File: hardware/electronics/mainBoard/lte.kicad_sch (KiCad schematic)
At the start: 39 parts, among them J10 M.2 Standoff, J8 Bus_M.2_Socket_E, J9 M.2 Standoff, SW5 JS102011JCQN, SW6 JS102011JCQN, U10 TPS22996H-Q1, U11 TXS0108EQWRKSRQ1, U12 TXS0104VxRUTR

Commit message: redefined symbol refs
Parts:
- renumbered D7 to D5, JP4 to JP2, R41 to R39, R42 to R40, R43 to R41, R44 to R42
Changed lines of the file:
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@@
 		(dnp no)
 		(fields_autoplaced yes)
-		(property "Reference" "#PWR0147"
+		(property "Reference" "#PWR0145"
 			(at 55.88 184.15 0)
 			(effects
@@
 			(project "mainBoard"
 				(path "/be16e32f-2ccf-4272-9ec7-94d5fe7a55e0/7ff6c767-11c2-4c6d-a16f-82c26617ef6d"
-					(reference "#PWR0147")
+					(reference "#PWR0145")
 					(unit 1)
 				)
@@
 		(dnp no)
 		(fields_autoplaced yes)
-		(property "Reference" "#PWR0150"
+		(property "Reference" "#PWR0148"
 			(at 127 191.77 0)
 			(effects
@@
 			(project "mainBoard"
 				(path "/be16e32f-2ccf-4272-9ec7-94d5fe7a55e0/7ff6c767-11c2-4c6d-a16f-82c26617ef6d"
-					(reference "#PWR0150")
+					(reference "#PWR0148")
 					(unit 1)
 				)
@@
 		(dnp no)
 		(fields_autoplaced yes)
-		(property "Reference" "#PWR0151"
+		(property "Reference" "#PWR0149"
 			(at 152.4 191.77 0)
 			(effects
@@
 			(project "mainBoard"
 				(path "/be16e32f-2ccf-4272-9ec7-94d5fe7a55e0/7ff6c767-11c2-4c6d-a16f-82c26617ef6d"
-					(reference "#PWR0151")
+					(reference "#PWR0149")
 					(unit 1)
 				)
@@
 		(dnp no)
 		(fields_autoplaced yes)
-		(property "Reference" "#PWR0130"
+		(property "Reference" "#PWR0129"
 			(at 200.66 27.94 0)
 			(effects
@@
 			(project "mainBoard"
 				(path "/be16e32f-2ccf-4272-9ec7-94d5fe7a55e0/7ff6c767-11c2-4c6d-a16f-82c26617ef6d"
-					(reference "#PWR0130")
+					(reference "#PWR0129")
 					(unit 1)
 				)
@@
 		(dnp no)
 		(fields_autoplaced yes)
-		(property "Reference" "#PWR0131"
+		(property "Reference" "#PWR0130"
 			(at 180.34 30.48 0)
 			(effects
@@
 			(project ""
 				(path "/be16e32f-2ccf-4272-9ec7-94d5fe7a55e0/7ff6c767-11c2-4c6d-a16f-82c26617ef6d"
-					(reference "#PWR0131")
+					(reference "#PWR0130")
 					(unit 1)
 				)
@@
 		(dnp no)
 		(fields_autoplaced yes)
-		(property "Reference" "#PWR0145"
+		(property "Reference" "#PWR0143"
 			(at 139.7 157.48 0)
 			(effects
@@
 			(project "mainBoard"
 				(path "/be16e32f-2ccf-4272-9ec7-94d5fe7a55e0/7ff6c767-11c2-4c6d-a16f-82c26617ef6d"
-					(reference "#PWR0145")
+					(reference "#PWR0143")
 					(unit 1)
 				)
@@
 		(dnp no)
 		(fields_autoplaced yes)
-		(property "Reference" "R42"
+		(property "Reference" "R40"
 			(at 199.39 34.29 0)
 			(do_not_autoplace yes)
@@
 			(project "mainBoard"
 				(path "/be16e32f-2ccf-4272-9ec7-94d5fe7a55e0/7ff6c767-11c2-4c6d-a16f-82c26617ef6d"
-					(reference "R42")
+					(reference "R40")
 					(unit 1)
 				)
@@
 		(dnp no)
 		(fields_autoplaced yes)
-		(property "Reference" "#PWR0148"
+		(property "Reference" "#PWR0146"
 			(at 30.48 191.77 0)
 			(effects
@@
 			(project "mainBoard"
 				(path "/be16e32f-2ccf-4272-9ec7-94d5fe7a55e0/7ff6c767-11c2-4c6d-a16f-82c26617ef6d"
-					(reference "#PWR0148")
+					(reference "#PWR0146")
 					(unit 1)
 				)
@@
 		(dnp no)
 		(fields_autoplaced yes)
-		(property "Reference" "#PWR0146"
+		(property "Reference" "#PWR0144"
 			(at 30.48 184.15 0)
 			(effects
@@
 			(project "mainBoard"
 				(path "/be16e32f-2ccf-4272-9ec7-94d5fe7a55e0/7ff6c767-11c2-4c6d-a16f-82c26617ef6d"
-					(reference "#PWR0146")
+					(reference "#PWR0144")
 					(unit 1)
 				)
@@
 		(dnp no)
 		(fields_autoplaced yes)
-		(property "Reference" "#PWR0129"
+		(property "Reference" "#PWR0128"
 			(at 203.2 19.05 0)
 			(effects
@@
 			(project ""
 				(path "/be16e32f-2ccf-4272-9ec7-94d5fe7a55e0/7ff6c767-11c2-4c6d-a16f-82c26617ef6d"
-					(reference "#PWR0129")
+					(reference "#PWR0128")
 					(unit 1)
 				)
@@
 		(dnp no)
 		(fields_autoplaced yes)
-		(property "Reference" "#PWR0149"
+		(property "Reference" "#PWR0147"
 			(at 55.88 191.77 0)
 			(effects
@@
 			(project "mainBoard"
 				(path "/be16e32f-2ccf-4272-9ec7-94d5fe7a55e0/7ff6c767-11c2-4c6d-a16f-82c26617ef6d"
-					(reference "#PWR0149")
+					(reference "#PWR0147")
 					(unit 1)
 				)
@@
 		(dnp no)
 		(fields_autoplaced yes)
-		(property "Reference" "D7"
+		(property "Reference" "D5"
 			(at 255.27 38.735 0)
 			(do_not_autoplace yes)
@@
 			(project "mainBoard"
 				(path "/be16e32f-2ccf-4272-9ec7-94d5fe7a55e0/7ff6c767-11c2-4c6d-a16f-82c26617ef6d"
-					(reference "D7")
+					(reference "D5")
 					(unit 1)
 				)
@@
 		(dnp no)
 		(fields_autoplaced yes)
-		(property "Reference" "R43"
+		(property "Reference" "R41"
 			(at 199.39 44.45 0)
 			(do_not_autoplace yes)
@@
 			(project "mainBoard"
 				(path "/be16e32f-2ccf-4272-9ec7-94d5fe7a55e0/7ff6c767-11c2-4c6d-a16f-82c26617ef6d"
-					(reference "R43")
+					(reference "R41")
 					(unit 1)
 				)
@@
 		(on_board yes)
 		(dnp no)
-		(property "Reference" "JP4"
+		(property "Reference" "JP2"
 			(at 255.27 55.88 90)
 			(do_not_autoplace yes)
@@
 			(project "mainBoard"
 				(path "/be16e32f-2ccf-4272-9ec7-94d5fe7a55e0/7ff6c767-11c2-4c6d-a16f-82c26617ef6d"
-					(reference "JP4")
+					(reference "JP2")
 					(unit 1)
 				)
@@
 		(dnp no)
 		(fields_autoplaced yes)
-		(property "Reference" "R41"
+		(property "Reference" "R39"
 			(at 88.9 25.4 0)
 			(do_not_autoplace yes)
@@
 			(project "mainBoard"
 				(path "/be16e32f-2ccf-4272-9ec7-94d5fe7a55e0/7ff6c767-11c2-4c6d-a16f-82c26617ef6d"
-					(reference "R41")
+					(reference "R39")
 					(unit 1)
 				)
@@
 		(dnp no)
 		(fields_autoplaced yes)
-		(property "Reference" "#PWR0120"
+		(property "Reference" "#PWR0131"
 			(at 228.6 40.64 0)
 			(effects
@@
 			(project "mainBoard"
 				(path "/be16e32f-2ccf-4272-9ec7-94d5fe7a55e0/7ff6c767-11c2-4c6d-a16f-82c26617ef6d"
-					(reference "#PWR0120")
+					(reference "#PWR0131")
 					(unit 1)
 				)
@@
 		(dnp no)
 		(fields_autoplaced yes)
-		(property "Reference" "R44"
+		(property "Reference" "R42"
 			(at 255.27 45.72 0)
 			(do_not_autoplace yes)
@@
 			(project "mainBoard"
 				(path "/be16e32f-2ccf-4272-9ec7-94d5fe7a55e0/7ff6c767-11c2-4c6d-a16f-82c26617ef6d"
-					(reference "R44")
+					(reference "R42")
 					(unit 1)
 				)

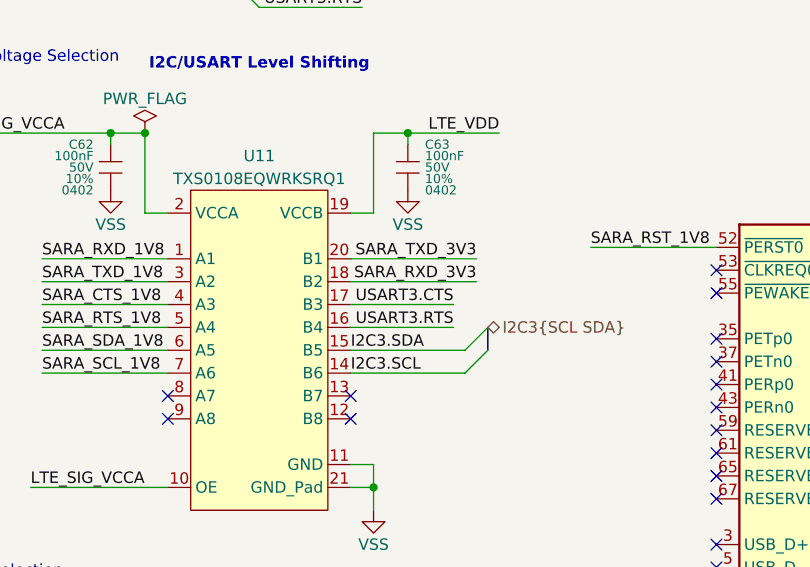
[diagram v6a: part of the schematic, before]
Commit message: fixed rx/tx
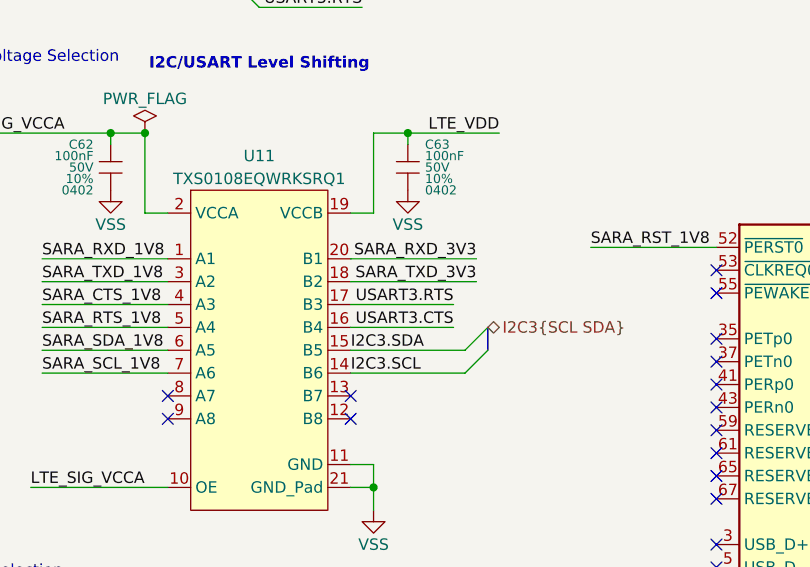
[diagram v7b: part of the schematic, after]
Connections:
- net SARA_RXD_3V3: now also U11.20 (B1); no longer U11.18 (B2)
- net SARA_TXD_3V3: now also U11.18 (B2); no longer U11.20 (B1)
- net USART3.CTS: now also U11.16 (B4); no longer U11.17 (B3)
- net USART3.RTS: now also U11.17 (B3); no longer U11.16 (B4)
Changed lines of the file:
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@@
-		)
-	)
-	(label "SARA_RXD_3V3"
-		(at 87.63 68.58 180)
-		(effects
-			(font
-				(size 1.27 1.27)
-			)
-			(justify right bottom)
 		)
 	)
@@
 		)
 	)
-	(label "USART3.RTS"
-		(at 85.09 73.66 180)
-		(effects
-			(font
-				(size 1.27 1.27)
-			)
-			(justify right bottom)
-		)
-	)
 	(label "LTE.SLEEP"
 		(at 86.36 125.73 180)
@@
 		)
 	)
-	(label "SARA_TXD_3V3"
-		(at 87.63 66.04 180)
-		(effects
-			(font
-				(size 1.27 1.27)
-			)
-			(justify right bottom)
-		)
-	)
 	(label "SARA_RST_1V8"
 		(at 100.33 64.77 0)
@@
 		)
 	)
+	(label "USART3.RTS"
+		(at 85.09 71.12 180)
+		(effects
+			(font
+				(size 1.27 1.27)
+			)
+			(justify right bottom)
+		)
+	)
 	(label "SARA_SCL_1V8"
 		(at 39.37 179.07 180)
@@
 		)
 	)
+	(label "SARA_TXD_3V3"
+		(at 87.63 68.58 180)
+		(effects
+			(font
+				(size 1.27 1.27)
+			)
+			(justify right bottom)
+		)
+	)
 	(label "LTE_1V8"
 		(at 236.22 35.56 180)
@@
 		)
 	)
+	(label "USART3.CTS"
+		(at 85.09 73.66 180)
+		(effects
+			(font
+				(size 1.27 1.27)
+			)
+			(justify right bottom)
+		)
+	)
 	(label "SARA_SLEEP_1V8"
 		(at 34.29 125.73 0)
@@
 		)
 	)
-	(label "USART3.CTS"
-		(at 85.09 71.12 180)
-		(effects
-			(font
-				(size 1.27 1.27)
-			)
-			(justify right bottom)
-		)
-	)
 	(label "LTE.NET_STS"
 		(at 40.64 26.67 180)
@@
 		(effects
 			(font
+				(size 1.27 1.27)
+			)
+			(justify right bottom)
+		)
+	)
+	(label "SARA_RXD_3V3"
+		(at 87.63 66.04 180)
+		(effects
+			(font

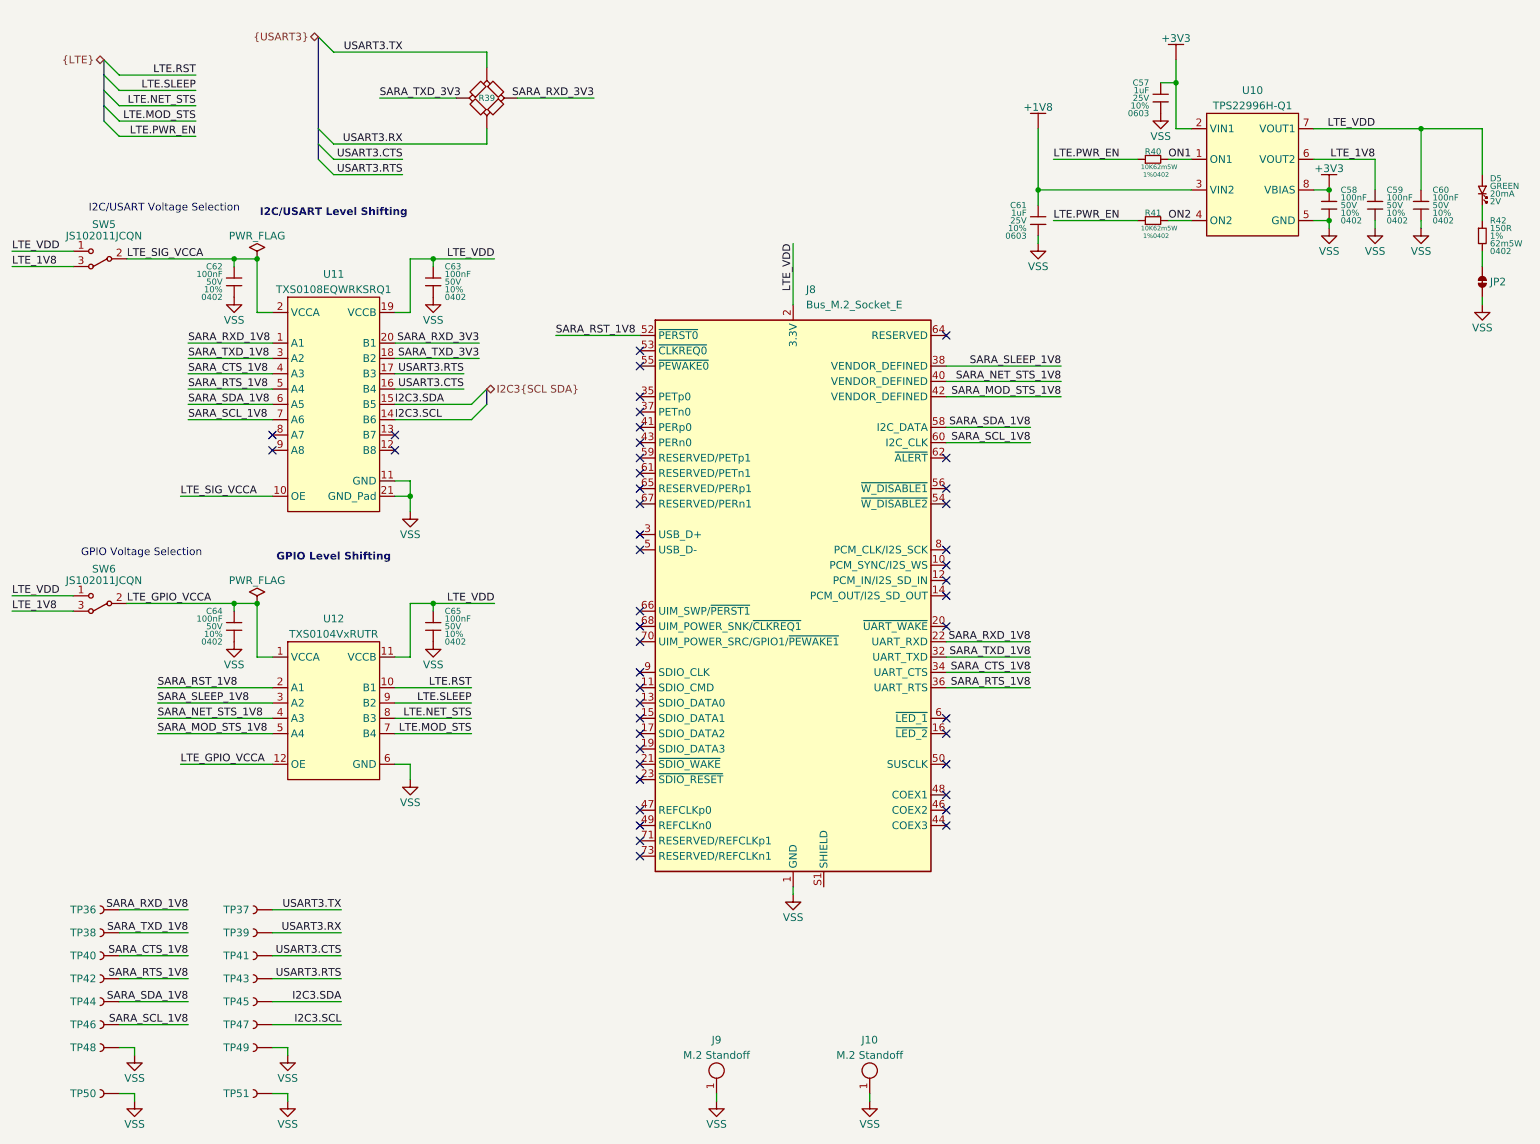
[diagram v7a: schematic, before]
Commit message: fixed net names and added notes
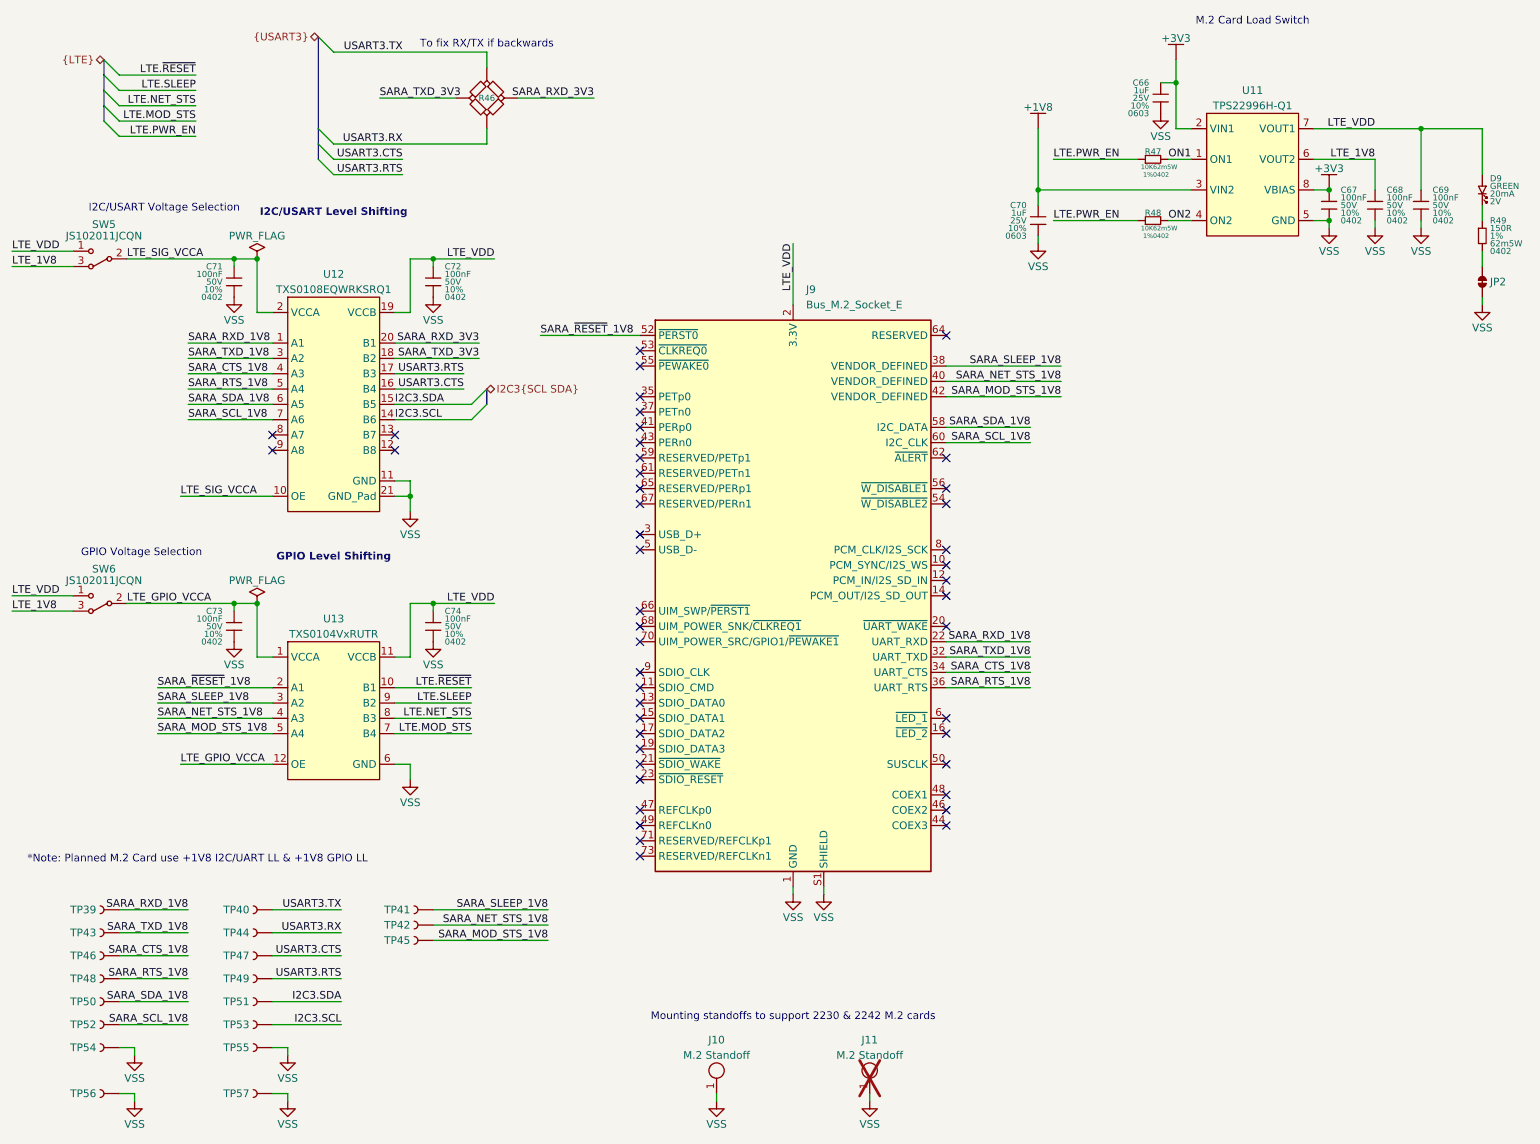
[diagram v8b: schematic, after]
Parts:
- removed R39: ~, lib_passives:CRCW0402_QUAD_UART, symbol lib_sch:R_double
- added R46: 0R, lib_passives:CRCW0402_QUAD_UART, symbol lib_sch:R_double
- added TP41, TP42, TP45: RCWCTE, lib_misc:TP_RCW, symbol lib_sch:Testpoint
- J11: renamed from J10; now not fitted
- renumbered C57 to C66, C58 to C67, C59 to C68, C60 to C69, C61 to C70, C62 to C71, C63 to C72, C64 to C73, C65 to C74, D5 to D9, J9 to J10, J8 to J9, R40 to R47, R41 to R48, R42 to R49, TP36 to TP39, TP37 to TP40, TP38 to TP43, TP39 to TP44, TP40 to TP46, TP41 to TP47, TP42 to TP48, TP43 to TP49, TP44 to TP50, TP45 to TP51, TP46 to TP52, TP47 to TP53, TP48 to TP54, TP49 to TP55, TP50 to TP56, TP51 to TP57, U10 to U11, U11 to U12, U12 to U13
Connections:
- net SARA_MOD_STS_1V8: now also TP45.1
- net SARA_NET_STS_1V8: now also TP42.1
- net SARA_RXD_3V3: now also R46.2
- net SARA_SLEEP_1V8: now also TP41.1
- net SARA_TXD_3V3: now also R46.4
- net USART3.RX: now also R46.3
- net USART3.TX: now also R46.1
- net VSS: now also J9.S1 (SHIELD), J9.S2 (SHIELD)
- net LTE.RST renamed LTE.~{RESET}
- net SARA_RST_1V8 renamed SARA_~{RESET}_1V8
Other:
- note added: "*Note: Planned M.2 Card use +1V8 I2C/UART LL & +1V8 GPIO LL"
- note added: "M.2 Card Load Switch"
- note added: "Mounting standoffs to support 2230 & 2242 M.2 cards"
- note added: "To fix RX/TX if backwards"
